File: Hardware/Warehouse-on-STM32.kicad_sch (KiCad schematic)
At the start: 1 part, among them U1 STM32F100C8Tx

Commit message: i
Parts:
- added C1, C2: 33pF, symbol Device:C
- added Y2: Crystal, symbol Device:Crystal
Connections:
- net GND: now also C1.2, C2.2
- net BOOT1: now reaches U1.20 (PB2)
- net BOOT0: now reaches U1.44 (BOOT0)
- net at U1.5 (PD0): now also C1.1, Y2.1
- net at U1.6 (PD1): now also C2.1, Y2.2
- net RESET: now reaches U1.7 (NRST)
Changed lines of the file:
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@@
   (junction (at 171.45 124.46) (diameter 0) (color 0 0 0 0)
   )
+  (junction (at 97.79 64.77) (diameter 0) (color 0 0 0 0)
+  )
+  (junction (at 104.14 74.93) (diameter 0) (color 0 0 0 0)
+  )
   (junction (at 176.53 43.18) (diameter 0) (color 0 0 0 0)
   )
+  (junction (at 110.49 64.77) (diameter 0) (color 0 0 0 0)
+  )
   (junction (at 168.91 43.18) (diameter 0) (color 0 0 0 0)
   )
@@
   (junction (at 171.45 43.18) (diameter 0) (color 0 0 0 0)
   )
+  (wire (pts (xy 156.21 62.23) (xy 110.49 62.23))
+    (stroke (width 0) (type default))
+  )
   (wire (pts (xy 173.99 123.19) (xy 173.99 124.46))
     (stroke (width 0) (type default))
@@
     (stroke (width 0) (type default))
   )
+  (wire (pts (xy 97.79 74.93) (xy 104.14 74.93))
+    (stroke (width 0) (type default))
+  )
+  (wire (pts (xy 97.79 57.15) (xy 110.49 57.15))
+    (stroke (width 0) (type default))
+  )
   (wire (pts (xy 173.99 44.45) (xy 173.99 43.18))
     (stroke (width 0) (type default))
   )
+  (wire (pts (xy 156.21 59.69) (xy 110.49 59.69))
+    (stroke (width 0) (type default))
+  )
+  (wire (pts (xy 147.32 49.53) (xy 156.21 49.53))
+    (stroke (width 0) (type default))
+  )
+  (wire (pts (xy 97.79 57.15) (xy 97.79 64.77))
+    (stroke (width 0) (type default))
+  )
+  (wire (pts (xy 110.49 62.23) (xy 110.49 64.77))
+    (stroke (width 0) (type default))
+  )
+  (wire (pts (xy 110.49 74.93) (xy 110.49 73.66))
+    (stroke (width 0) (type default))
+  )
+  (wire (pts (xy 110.49 64.77) (xy 107.95 64.77))
+    (stroke (width 0) (type default))
+  )
+  (wire (pts (xy 110.49 59.69) (xy 110.49 57.15))
+    (stroke (width 0) (type default))
+  )
+  (wire (pts (xy 104.14 74.93) (xy 104.14 76.2))
+    (stroke (width 0) (type default))
+  )
+  (wire (pts (xy 97.79 73.66) (xy 97.79 74.93))
+    (stroke (width 0) (type default))
+  )
+  (wire (pts (xy 97.79 64.77) (xy 100.33 64.77))
+    (stroke (width 0) (type default))
+  )
   (wire (pts (xy 171.45 44.45) (xy 171.45 43.18))
     (stroke (width 0) (type default))
@@
     (stroke (width 0) (type default))
   )
+  (wire (pts (xy 104.14 74.93) (xy 110.49 74.93))
+    (stroke (width 0) (type default))
+  )
+  (wire (pts (xy 147.32 82.55) (xy 156.21 82.55))
+    (stroke (width 0) (type default))
+  )
   (wire (pts (xy 173.99 43.18) (xy 176.53 43.18))
     (stroke (width 0) (type default))
@@
     (stroke (width 0) (type default))
   )
+  (wire (pts (xy 147.32 54.61) (xy 156.21 54.61))
+    (stroke (width 0) (type default))
+  )
+  (wire (pts (xy 110.49 64.77) (xy 110.49 66.04))
+    (stroke (width 0) (type default))
+  )
+  (wire (pts (xy 97.79 66.04) (xy 97.79 64.77))
+    (stroke (width 0) (type default))
+  )
   (wire (pts (xy 173.99 124.46) (xy 171.45 124.46))
     (stroke (width 0) (type default))
@@
     (stroke (width 0) (type default))
   )
+  (label "BOOT0" (at 147.32 54.61 0) (fields_autoplaced)
+    (effects (font (size 1.27 1.27)) (justify left bottom))
+  )
+  (label "BOOT1" (at 147.32 82.55 0) (fields_autoplaced)
+    (effects (font (size 1.27 1.27)) (justify left bottom))
+  )
+  (label "RESET" (at 147.32 49.53 0) (fields_autoplaced)
+    (effects (font (size 1.27 1.27)) (justify left bottom))
+  )
   (symbol (lib_id "power:GND") (at 171.45 125.73 0) (unit 1)
     (in_bom yes) (on_board yes) (dnp no) (fields_autoplaced)
@@
     )
   )
+  (symbol (lib_id "power:GND") (at 104.14 76.2 0) (unit 1)
+    (in_bom yes) (on_board yes) (dnp no) (fields_autoplaced)
+    (property "Reference" "#PWR03" (at 104.14 82.55 0)
+      (effects (font (size 1.27 1.27)) hide)
+    )
+    (property "Value" "GND" (at 104.14 81.28 0)
+      (effects (font (size 1.27 1.27)))
+    )
+    (property "Footprint" "" (at 104.14 76.2 0)
+      (effects (font (size 1.27 1.27)) hide)
+    )
+    (property "Datasheet" "" (at 104.14 76.2 0)
+      (effects (font (size 1.27 1.27)) hide)
+    )
+    (pin "1")
+    (instances
+      (project "Warehouse-on-STM32"
+        (path "/2599b9a9-6312-402b-9c24-1e87744a4c70"
+          (reference "#PWR03") (unit 1)
+        )
+      )
+    )
+  )
   (symbol (lib_id "power:+3V3") (at 168.91 41.91 0) (unit 1)
     (in_bom yes) (on_board yes) (dnp no) (fields_autoplaced)
@@
         (path "/2599b9a9-6312-402b-9c24-1e87744a4c70"
           (reference "#PWR01") (unit 1)
+        )
+      )
+    )
+  )
+  (symbol (lib_id "Device:C") (at 97.79 69.85 0) (unit 1)
+    (in_bom yes) (on_board yes) (dnp no) (fields_autoplaced)
+    (property "Reference" "C1" (at 101.6 69.215 0)
+      (effects (font (size 1.27 1.27)) (justify left))
+    )
+    (property "Value" "33pF" (at 101.6 71.755 0)
+      (effects (font (size 1.27 1.27)) (justify left))
+    )
+    (property "Footprint" "" (at 98.7552 73.66 0)
+      (effects (font (size 1.27 1.27)) hide)
+    )
+    (property "Datasheet" "~" (at 97.79 69.85 0)
+      (effects (font (size 1.27 1.27)) hide)
+    )
+    (pin "1")
+    (pin "2")
+    (instances
+      (project "Warehouse-on-STM32"
+        (path "/2599b9a9-6312-402b-9c24-1e87744a4c70"
+          (reference "C1") (unit 1)
         )
       )
@@
         )
       )
+    )
+  )
+  (symbol (lib_id "Device:C") (at 110.49 69.85 0) (unit 1)
+    (in_bom yes) (on_board yes) (dnp no) (fields_autoplaced)
+    (property "Reference" "C2" (at 114.3 69.215 0)
+      (effects (font (size 1.27 1.27)) (justify left))
+    )
+    (property "Value" "33pF" (at 114.3 71.755 0)
+      (effects (font (size 1.27 1.27)) (justify left))
+    )
+    (property "Footprint" "" (at 111.4552 73.66 0)
+      (effects (font (size 1.27 1.27)) hide)
+    )
+    (property "Datasheet" "~" (at 110.49 69.85 0)
+      (effects (font (size 1.27 1.27)) hide)
+    )
+    (pin "1")
+    (pin "2")
+    (instances
+      (project "Warehouse-on-STM32"
+        (path "/2599b9a9-6312-402b-9c24-1e87744a4c70"
+          (reference "C2") (unit 1)
+        )
+      )
+    )
+  )
+  (symbol (lib_id "Device:Crystal") (at 104.14 64.77 0) (unit 1)
+    (in_bom yes) (on_board yes) (dnp no) (fields_autoplaced)
+    (property "Reference" "Y2" (at 104.14 58.42 0)
+      (effects (font (size 1.27 1.27)))
+    )
+    (property "Value" "Crystal" (at 104.14 60.96 0)
+      (effects (font (size 1.27 1.27)))
+    )
+    (property "Footprint" "" (at 104.14 64.77 0)
+      (effects (font (size 1.27 1.27)) hide)
+    )
+    (property "Datasheet" "~" (at 104.14 64.77 0)
+      (effects (font (size 1.27 1.27)) hide)
+    )
+    (pin "1")
+    (pin "2")
+    (instances
+      (project "Warehouse-on-STM32"
+        (path "/2599b9a9-6312-402b-9c24-1e87744a4c70"
+          (reference "Y2") (unit 1)
+        )
+      )

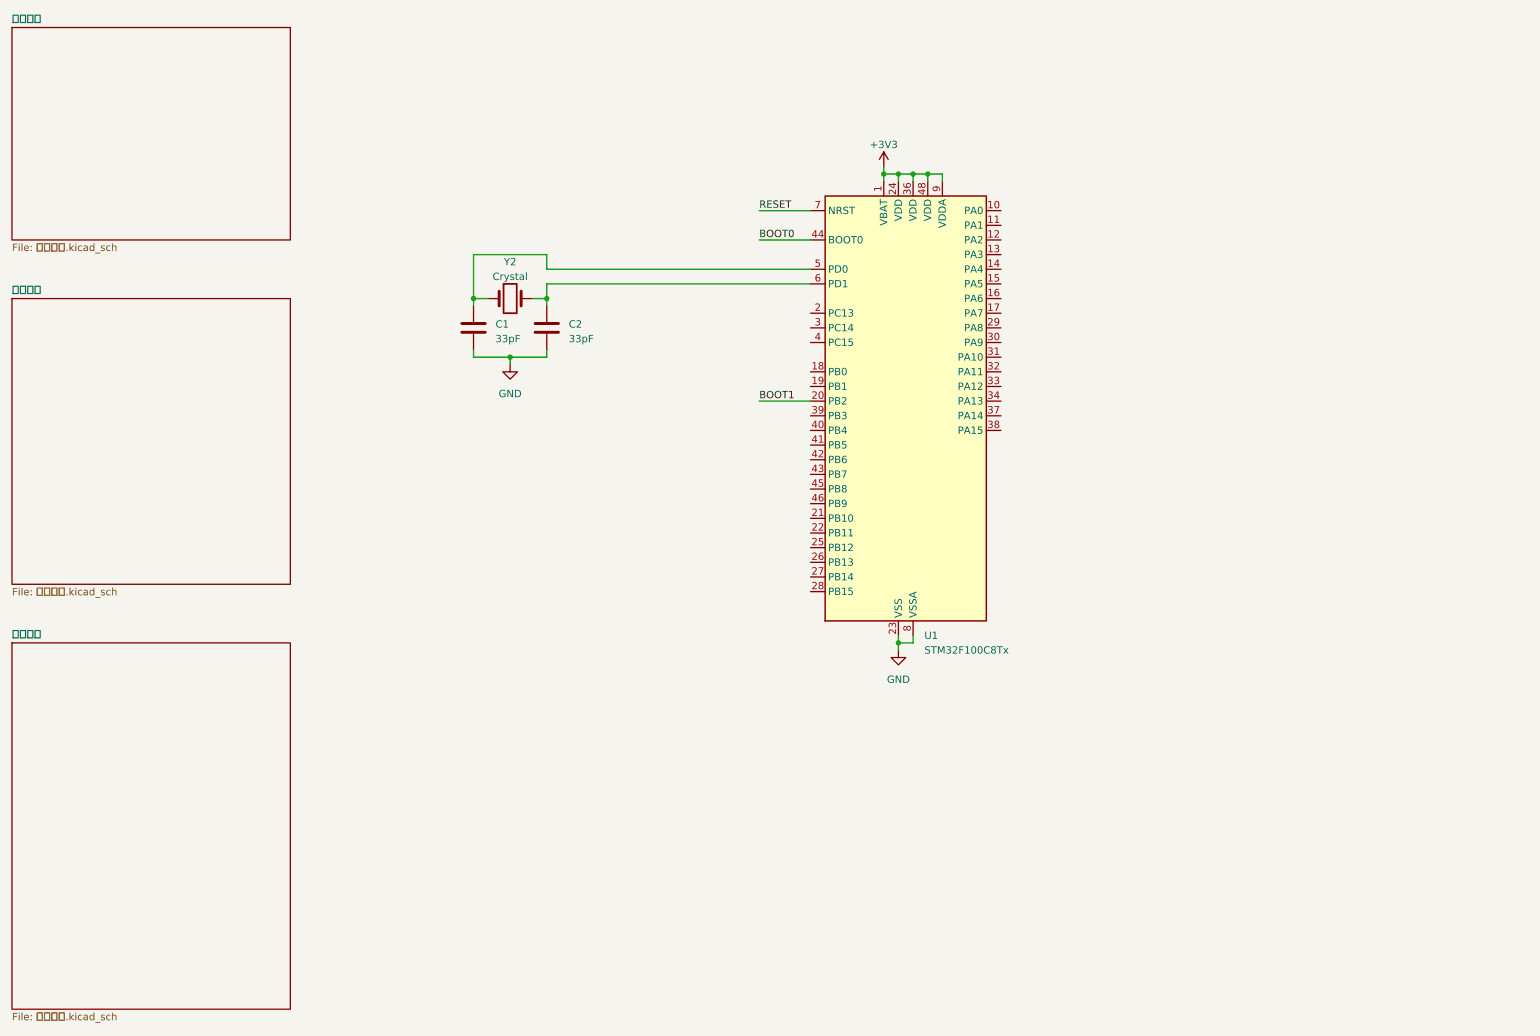
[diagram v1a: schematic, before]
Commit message: 完成最小系统的电路原理图设计
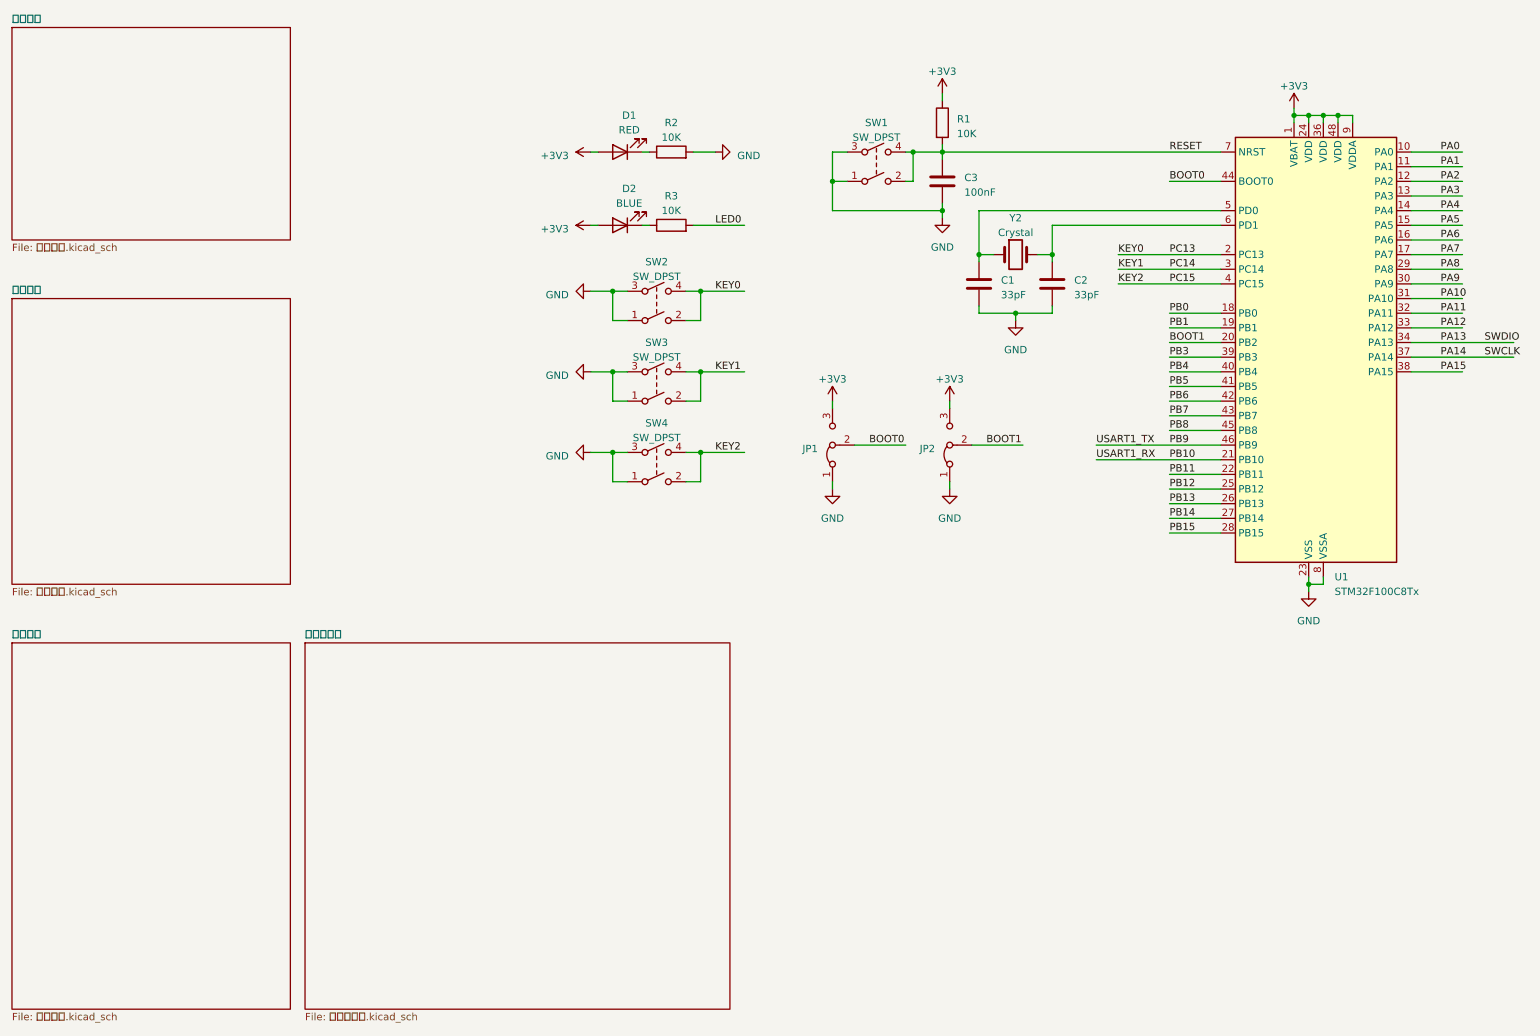
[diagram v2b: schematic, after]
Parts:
- added C3: 100nF, symbol Device:C
- added D1: RED, symbol Device:LED
- added D2: BLUE, symbol Device:LED
- added JP1, JP2: Jumper_3_Bridged12, symbol Jumper:Jumper_3_Bridged12
- added R1, R2, R3: 10K, symbol Device:R
- added SW1, SW2, SW3, SW4: SW_DPST, symbol Switch:SW_DPST
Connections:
- net +3V3: now also D1.2 (A), D2.2 (A), JP1.3 (B), JP2.3 (B), R1.1
- net BOOT0: now also JP1.2 (C)
- net BOOT1: now also JP2.2 (C)
- net GND: now also C3.2, JP1.1 (A), JP2.1 (A), R2.2, SW1.1, SW1.3, SW2.1, SW2.3, SW3.1, SW3.3, SW4.1, SW4.3
- net RESET: now also C3.1, R1.2, SW1.2, SW1.4
- net PA0: now reaches U1.10 (PA0)
- net PA1: now reaches U1.11 (PA1)
- net PA2: now reaches U1.12 (PA2)
- net PA3: now reaches U1.13 (PA3)
- net PA4: now reaches U1.14 (PA4)
- net PA5: now reaches U1.15 (PA5)
- net PA6: now reaches U1.16 (PA6)
- net PA7: now reaches U1.17 (PA7)
- net PB0: now reaches U1.18 (PB0)
- net PB1: now reaches U1.19 (PB1)
- net KEY0: now reaches U1.2 (PC13)
- net KEY0: now also SW2.2, SW2.4
- net PB10: now reaches U1.21 (PB10)
- net PB11: now reaches U1.22 (PB11)
- net PB12: now reaches U1.25 (PB12)
- net PB13: now reaches U1.26 (PB13)
- net PB14: now reaches U1.27 (PB14)
- net PB15: now reaches U1.28 (PB15)
- net PA8: now reaches U1.29 (PA8)
- net KEY1: now reaches U1.3 (PC14)
- net KEY1: now also SW3.2, SW3.4
- net PA9: now reaches U1.30 (PA9)
- net PA10: now reaches U1.31 (PA10)
- net PA11: now reaches U1.32 (PA11)
- net PA12: now reaches U1.33 (PA12)
- net PA13: now reaches U1.34 (PA13)
- net PA14: now reaches U1.37 (PA14)
- net PA15: now reaches U1.38 (PA15)
- net PB3: now reaches U1.39 (PB3)
- net KEY2: now reaches U1.4 (PC15)
- net KEY2: now also SW4.2, SW4.4
- net PB4: now reaches U1.40 (PB4)
- net PB5: now reaches U1.41 (PB5)
- net PB6: now reaches U1.42 (PB6)
- net PB7: now reaches U1.43 (PB7)
- net PB8: now reaches U1.45 (PB8)
- net PB9: now reaches U1.46 (PB9)
- new net: D1.1 (K), R2.1
- new net: D2.1 (K), R3.1
- new net LED0: R3.2
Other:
- added sheet 传感器模块 (传感器模块.kicad_sch)
- moved on the sheet: C1, C2, U1, Y2

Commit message: 运行DRC前
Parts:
- removed U1: STM32F100C8Tx, Package_QFP:LQFP-48_7x7mm_P0.5mm, symbol MCU_ST_STM32F1:STM32F100C8Tx
- added U1: STM32F103C8Tx, Package_QFP:LQFP-48_7x7mm_P0.5mm, symbol MCU_ST_STM32F1:STM32F103C8Tx
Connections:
- net +3V3: now also U1.1 (VBAT), U1.24 (VDD), U1.36 (VDD), U1.48 (VDD), U1.9 (VDDA)
- net BOOT0: now also U1.44 (BOOT0)
- net BOOT1: now also U1.20 (PB2)
- net GND: now also U1.23 (VSS), U1.35 (VSS), U1.47 (VSS), U1.8 (VSSA)
- net KEY0: now also U1.2 (PC13)
- net KEY1: now also U1.3 (PC14)
- net KEY2: now also U1.4 (PC15)
- net LED0: now also U1.11 (PA1)
- net PA13: now also U1.34 (PA13)
- net PA14: now also U1.37 (PA14)
- net PA15: now also U1.38 (PA15)
- net PA2: now also U1.12 (PA2), U1.46 (PB9)
- net PA3: now also U1.13 (PA3), U1.21 (PB10)
- net PA4: now also U1.14 (PA4)
- net PA5: now also U1.15 (PA5)
- net PA6: now also U1.16 (PA6)
- net PA7: now also U1.17 (PA7)
- net PA8: now also U1.29 (PA8)
- net PB0: now also U1.18 (PB0)
- net PB1: now also U1.19 (PB1)
- net PB11: now also U1.22 (PB11)
- net PB3: now also U1.39 (PB3)
- net PB4: now also U1.40 (PB4)
- net PB5: now also U1.41 (PB5)
- net PB6: now also U1.42 (PB6)
- net PB7: now also U1.43 (PB7)
- net PB8: now also U1.45 (PB8)
- net RESET: now also U1.7 (NRST)
- net at C1.1, Y2.1: now also U1.5 (PD0)
- net at C2.1, Y2.2: now also U1.6 (PD1)
- new net ADC: U1.10 (PA0)
- new net AIN10: U1.30 (PA9)
- new net AIN11: U1.25 (PB12)
- new net AIN20: U1.31 (PA10)
- new net AIN21: U1.26 (PB13)
- new net BIN10: U1.32 (PA11)
- new net BIN11: U1.27 (PB14)
- new net BIN20: U1.33 (PA12)
- new net BIN21: U1.28 (PB15)
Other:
- moved on the sheet: C1, C2, C3, D1, D2, JP1, JP2, R1, R2, R3, SW1, SW2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

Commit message: 2023/3/29
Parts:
- removed JP1, JP2: Jumper_3_Bridged12, symbol Jumper:Jumper_3_Bridged12
- removed SW1, SW2, SW3, SW4: SW_DPST, symbol Switch:SW_DPST
- added C10: 104, Capacitor_SMD:C_0402_1005Metric, symbol Device:C
- added C9: 10uF, Capacitor_SMD:C_0603_1608Metric, symbol Device:C
- added J1: ESP8266, Connector_PinSocket_2.54mm:PinSocket_2x04_P2.54mm_Vertical, symbol Connector_Generic:Conn_02x04_Counter_Clockwise
- added J2: Conn_01x05, Connector_PinHeader_2.54mm:PinHeader_1x05_P2.54mm_Vertical, symbol Connector_Generic:Conn_01x05
- added JP1, JP2: SolderJumper_3_Open, Jumper:SolderJumper-3_P2.0mm_Open_TrianglePad1.0x1.5mm, symbol Jumper:SolderJumper_3_Open
- added R3, R4: 10K, Resistor_SMD:R_0402_1005Metric, symbol Device:R
- added SW1, SW2, SW3, SW4: SW_Push, Button_Switch_SMD:SW_Tactile_SPST_NO_Straight_CK_PTS636Sx25SMTRLFS, symbol Switch:SW_Push
- C2: renamed from C3; value 100nF -> 104; footprint (none) -> Capacitor_SMD:C_0402_1005Metric
- C4: renamed from C1; footprint (none) -> Capacitor_SMD:C_0402_1005Metric
- C5: renamed from C2; footprint (none) -> Capacitor_SMD:C_0402_1005Metric
- D1, D2: footprint (none) -> LED_SMD:LED_0402_1005Metric
- R1: renamed from R2; footprint (none) -> Resistor_SMD:R_0402_1005Metric
- R2: renamed from R3; footprint (none) -> Resistor_SMD:R_0402_1005Metric
- R5: renamed from R1; footprint (none) -> Resistor_SMD:R_0402_1005Metric
- renumbered Y2 to Y1
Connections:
- net +3V3: now also C10.1, C9.1, J1.8 (Pin_8), JP1.3 (B), JP2.3 (B), R3.1, R4.1
- net BOOT0: now also JP1.2 (C)
- net BOOT1: now also JP2.2 (C)
- net GND: now also C10.2, C9.2, J1.4 (Pin_4), J2.3 (Pin_3), JP1.1 (A), JP2.1 (A), SW1.1, SW2.1, SW3.1, SW4.1
- net KEY0: now also SW1.2
- net KEY1: now also SW2.2
- net KEY2: now also SW3.2
- net RESET: now also SW4.2
- net AIN10 renamed BSLEEP
- net AIN11: no longer names the net of U1.25 (PB12)
- net AIN20 renamed BEN
- net AIN21: no longer names the net of U1.26 (PB13)
- net BIN10 renamed CSLEEP
- net BIN11: no longer names the net of U1.27 (PB14)
- net BIN20 renamed CEN
- net BIN21: no longer names the net of U1.28 (PB15)
- net PA13 renamed SWDIO
- net SWDIO: now also J2.1 (Pin_1)
- net PA14 renamed SWCLK
- net SWCLK: now also J2.2 (Pin_2)
- net PA15: no longer names the net of U1.38 (PA15)
- net PA2 renamed ESP_TX
- net ESP_TX: now also J1.5 (Pin_5); no longer U1.46 (PB9)
- net PA3 renamed ESP_RX
- net ESP_RX: now also J1.1 (Pin_1); no longer U1.21 (PB10)
- net PA4: no longer names the net of U1.14 (PA4)
- net PA5: no longer names the net of U1.15 (PA5)
- net PA6 renamed ASLEEP
- net PA7 renamed APH
- net PA8 renamed AEN
- net PB0: no longer names the net of U1.18 (PB0)
- net PB1: no longer names the net of U1.19 (PB1)
- net PB11: no longer names the net of U1.22 (PB11)
- net PB3: no longer names the net of U1.39 (PB3)
- net PB4: no longer names the net of U1.40 (PB4)
- net PB5: no longer names the net of U1.41 (PB5)
- net PB6 renamed SCL
- net PB7 renamed SDA
- net PB8: no longer names the net of U1.45 (PB8)
- new net: J1.6 (Pin_6), R4.2
- new net: J1.7 (Pin_7), R3.2
- new net USART1_RX: J2.5 (Pin_5), U1.21 (PB10)
- new net USART1_TX: J2.4 (Pin_4), U1.46 (PB9)
- no-connect marks 0 -> 16
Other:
- removed sheet 通信模块
- sheet 传感器模块 ports: added ADC, SCL, SDA; removed none
- sheet 驱动模块 ports: added AEN, APH, ASLEEP, BEN, BSLEEP, CEN, CSLEEP; removed none

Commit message: nm
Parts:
- Y1: footprint (none) -> Crystal:Crystal_SMD_5032-2Pin_5.0x3.2mm
- renumbered C2 to C3, R3 to R1, R4 to R2, R1 to R3, R2 to R4
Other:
- moved on the sheet: C10, C9, D1, D2, J1, R1, R2, R3, R4, SW1, SW2, SW3

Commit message: nm
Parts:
- removed JP1, JP2: SolderJumper_3_Open, Jumper:SolderJumper-3_P2.0mm_Open_TrianglePad1.0x1.5mm, symbol Jumper:SolderJumper_3_Open
- added C10: 104, Capacitor_SMD:C_0402_1005Metric, symbol Device:C
- added C9: 10uF, Capacitor_SMD:C_0402_1005Metric, symbol Device:C
- renumbered C4 to C5, C5 to C7
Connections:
- net BOOT0 is gone; now on net GND: U1.44 (BOOT0)
- net BOOT1 is gone; now on net GND: U1.20 (PB2)
- net +3V3: now also C10.1, C9.1
- net GND: now also C10.2, C9.2

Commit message: 完成布局
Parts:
- removed Y1: Crystal, Crystal:Crystal_SMD_5032-2Pin_5.0x3.2mm, symbol Device:Crystal
- added Y1: 8MHz, Crystal:Crystal_SMD_3225-4Pin_3.2x2.5mm, symbol Device:Crystal_GND24_Small
- C9: footprint Capacitor_SMD:C_0603_1608Metric -> Capacitor_SMD:C_0402_1005Metric
- J2: footprint Connector_PinHeader_2.54mm:PinHeader_1x05_P2.54mm_Vertical -> Connector_PinHeader_1.00mm:PinHeader_1x05_P1.00mm_Vertical
- SW1, SW2, SW3, SW4: footprint Button_Switch_SMD:SW_Tactile_SPST_NO_Straight_CK_PTS636Sx25SMTRLFS -> Button_Switch_SMD:SW_XKB_TS-1185-B-A-B-A
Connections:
- net AEN: now also U1.4 (PC15); no longer U1.29 (PA8)
- net APH: now also U1.3 (PC14); no longer U1.17 (PA7)
- net ASLEEP: now also U1.2 (PC13); no longer U1.16 (PA6)
- net BEN: now also U1.41 (PB5); no longer U1.31 (PA10)
- net BSLEEP: now also U1.40 (PB4); no longer U1.30 (PA9)
- net CEN: now also U1.39 (PB3); no longer U1.33 (PA12)
- net CSLEEP: now also U1.38 (PA15); no longer U1.32 (PA11)
- net GND: now also Y1.2, Y1.4
- net KEY0: now also U1.16 (PA6); no longer U1.2 (PC13)
- net KEY1: now also U1.15 (PA5); no longer U1.3 (PC14)
- net KEY2: now also U1.14 (PA4); no longer U1.4 (PC15)
- net SWCLK: now also J2.1 (Pin_1); no longer J2.2 (Pin_2)
- net SWDIO: now also J2.2 (Pin_2); no longer J2.1 (Pin_1)
- net USART1_RX: now also J2.4 (Pin_4), U1.31 (PA10); no longer J2.5 (Pin_5), U1.21 (PB10)
- net USART1_TX: now also J2.5 (Pin_5), U1.30 (PA9); no longer J2.4 (Pin_4), U1.46 (PB9)
- net at C5.1, U1.5 (PD0): now also Y1.1
- net at C7.1, U1.6 (PD1): now also Y1.3
